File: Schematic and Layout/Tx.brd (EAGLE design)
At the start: 76.2 x 63.5 mm, 31 parts

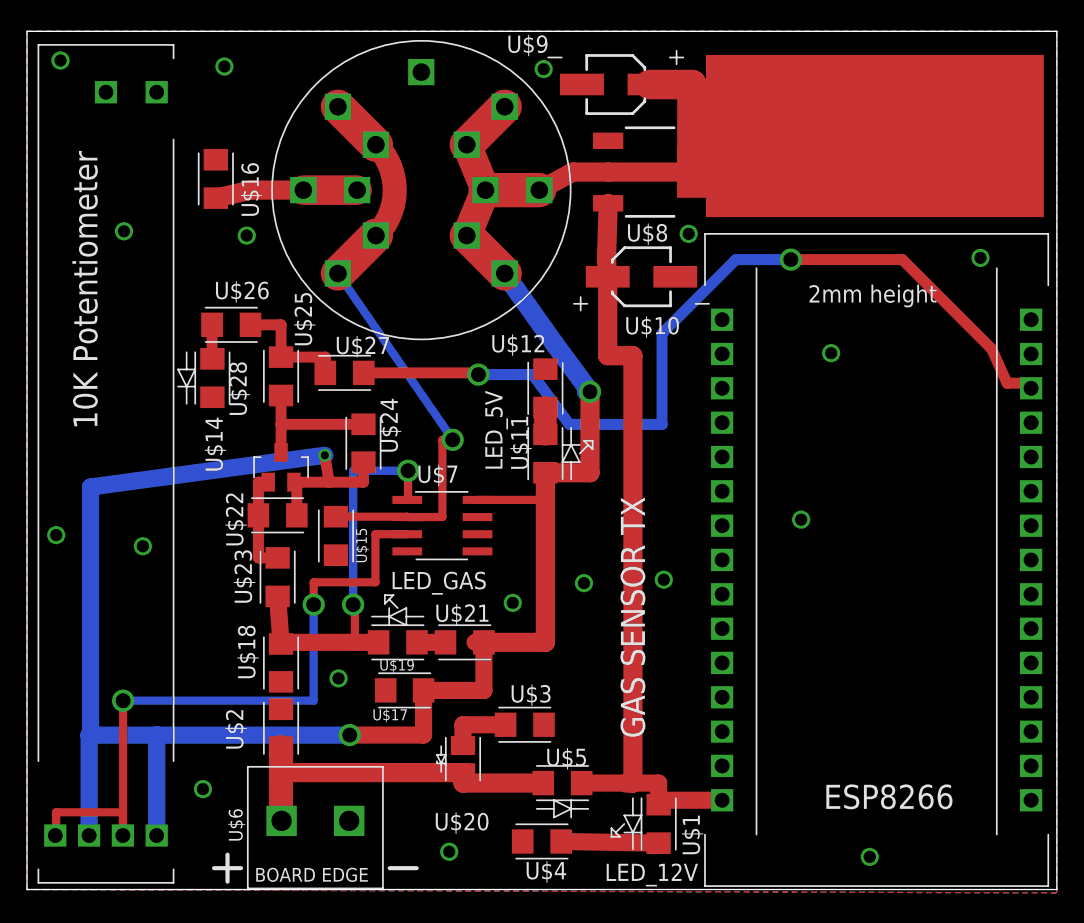
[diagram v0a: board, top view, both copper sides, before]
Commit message: ESPs now run off of 5 V
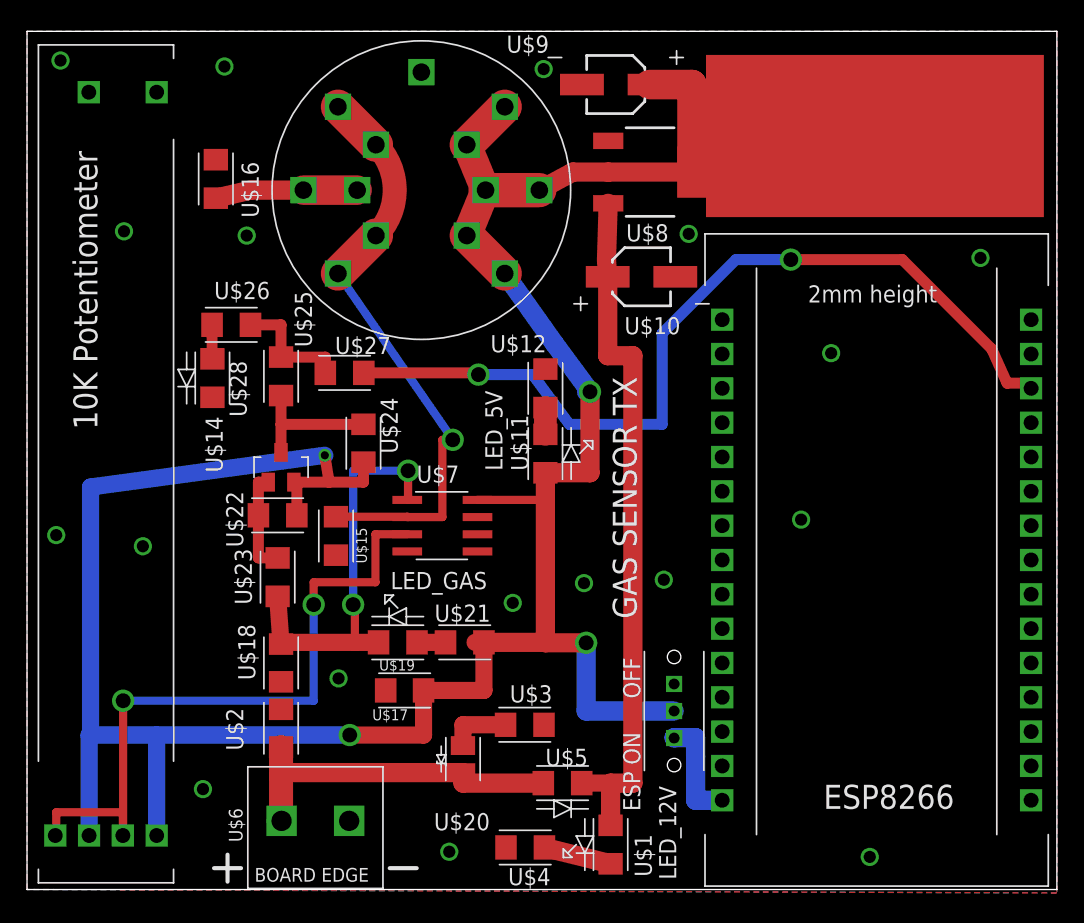
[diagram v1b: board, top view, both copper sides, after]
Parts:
- added U$32: SPDT, Gas_Sensor_Lib_v1:SPDT
- moved U$1 3.87 mm to (43.2, 3.33)
- moved U$4 1.32 mm to (36.9, 3.11)
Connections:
- new net ESP_VIN: U$29.VIN, U$32.A
- net 12V: no longer U$29.VIN
- net 5V: now also U$32.IN
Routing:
- net 5V: track 198.5 -> 213.0 mm, vias 3 -> 4
- net ESP_VIN: track 0.00 -> 8.25 mm
- net 12V: track 57.3 -> 52.8 mm
- net N$2: track 7.22 -> 5.04 mm
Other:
- board text added: "TRANSCEIVER - TX CAPSTONE SPRING 2017"
- board text removed: "TRANCEIVER - TX CAPSTONE SPRING 2017"
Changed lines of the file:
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@@
 <setting verticaltext="up"/>
 </settings>
-<grid distance="0.0025" unitdist="inch" unit="inch" style="dots" multiple="1" display="yes" altdistance="0.025" altunitdist="inch" altunit="inch"/>
+<grid distance="0.00125" unitdist="inch" unit="inch" style="dots" multiple="1" display="yes" altdistance="0.025" altunitdist="inch" altunit="inch"/>
 <layers>
 <layer number="1" name="Top" color="4" fill="1" visible="yes" active="yes"/>
@@
 <text x="5.207" y="34.036" size="1.778" layer="21" rot="R90">10K Potentiometer</text>
 <text x="58.928" y="5.969" size="1.778" layer="21">ESP8266</text>
-<text x="45.72" y="11.176" size="1.778" layer="21" rot="R90">GAS SENSOR TX</text>
-<text x="70.358" y="38.608" size="1.778" layer="22" rot="MR270">TRANCEIVER - TX
+<text x="45.11675" y="20.03425" size="1.778" layer="21" rot="R90">GAS SENSOR TX</text>
+<text x="70.358" y="38.608" size="1.778" layer="22" rot="MR270">TRANSCEIVER - TX
 CAPSTONE SPRING 2017</text>
 <text x="65.024" y="19.558" size="1.778" layer="22" rot="MR270">Alec
@@
 Kam
 Noah</text>
-<text x="42.7355" y="0.635" size="1.27" layer="21">LED_12V</text>
+<text x="48.03775" y="0.73025" size="1.27" layer="21" rot="R90">LED_12V</text>
 <text x="35.179" y="30.988" size="1.27" layer="21" rot="R90">LED_5V</text>
 <text x="34.036" y="23.495" size="1.27" layer="21" rot="R180">LED_GAS</text>
@@
 </autorouter>
 <elements>
-<element name="U$1" library="Gas_Sensor_Lib_v1" package="LED_1206" value="LED_12V" x="46.736" y="4.851" smashed="yes" rot="R270">
-<attribute name="NAME" x="48.514" y="5.613" size="1.27" layer="25" rot="R270"/>
-<attribute name="VALUE" x="42.647" y="0.635" size="1.27" layer="27"/>
+<element name="U$1" library="Gas_Sensor_Lib_v1" package="LED_1206" value="LED_12V" x="43.18" y="3.327" smashed="yes" rot="R270">
+<attribute name="NAME" x="44.958" y="4.089" size="1.27" layer="25" rot="R270"/>
+<attribute name="VALUE" x="49.911" y="0.76875" size="1.27" layer="27" rot="R90"/>
 </element>
 <element name="U$2" library="Gas_Sensor_Lib_v1" package="C1206" value="10uF" x="18.796" y="11.938" smashed="yes" rot="R90">
@@
 <attribute name="VALUE" x="42.164" y="14.478" size="1.27" layer="27" rot="R180"/>
 </element>
-<element name="U$4" library="Gas_Sensor_Lib_v1" package="R1206" value="1K" x="38.1" y="3.556" smashed="yes">
-<attribute name="NAME" x="36.83" y="0.762" size="1.27" layer="25"/>
-<attribute name="VALUE" x="34.163" y="0.762" size="1.27" layer="27"/>
+<element name="U$4" library="Gas_Sensor_Lib_v1" package="R1206" value="1K" x="36.86175" y="3.1115" smashed="yes">
+<attribute name="NAME" x="35.59175" y="0.3175" size="1.27" layer="25"/>
+<attribute name="VALUE" x="32.92475" y="0.3175" size="1.27" layer="27"/>
 </element>
 <element name="U$5" library="Gas_Sensor_Lib_v1" package="DIDOE_1206" value="DIODE" x="39.624" y="7.874" smashed="yes">
@@
 <element name="U$30" library="Gas_Sensor_Lib_v1" package="POTENTIOMETER" value="POTENTIOMETER" x="5.842" y="31.496" smashed="yes" rot="R90"/>
 <element name="U$31" library="Gas_Sensor_Lib_v1" package="THERMAL" value="HEAT_SINK" x="62.738" y="55.753"/>
+<element name="U$32" library="Gas_Sensor_Lib_v1" package="SPDT" value="SPDT" x="47.879" y="13.208" rot="R90"/>
 </elements>
 <signals>
@@
 <contactref element="U$8" pad="3"/>
 <contactref element="U$10" pad="+"/>
-<contactref element="U$29" pad="VIN"/>
-<wire x1="44.323" y1="7.874" x2="46.736" y2="7.874" width="1.27" layer="1"/>
-<wire x1="44.323" y1="7.874" x2="41.046" y2="7.874" width="1.27" layer="1"/>
-<wire x1="46.736" y1="6.604" x2="46.736" y2="7.874" width="1.27" layer="1"/>
-<wire x1="51.435" y1="6.604" x2="46.736" y2="6.604" width="1.27" layer="1"/>
-<wire x1="46.736" y1="6.604" x2="46.736" y2="6.273" width="1.27" layer="1"/>
+<wire x1="41.046" y1="7.874" x2="44.323" y2="7.874" width="1.27" layer="1"/>
 <wire x1="42.8752" y1="46.5728" x2="42.966" y2="45.339" width="1.4224" layer="1"/>
 <wire x1="42.8752" y1="46.5728" x2="43.0022" y2="50.7746" width="1.4224" layer="1"/>
@@
 <wire x1="44.831" y1="39.497" x2="44.831" y2="7.874" width="1.4224" layer="1"/>
 <wire x1="44.831" y1="7.874" x2="44.323" y2="7.874" width="1.4224" layer="1"/>
+<wire x1="44.323" y1="7.874" x2="43.18" y2="7.874" width="1.4224" layer="1"/>
+<wire x1="43.18" y1="7.874" x2="43.18" y2="4.749" width="1.4224" layer="1"/>
 </signal>
 <signal name="N$2">
 <contactref element="U$1" pad="2"/>
 <contactref element="U$4" pad="2"/>
-<wire x1="46.736" y1="3.429" x2="39.522" y2="3.556" width="1.27" layer="1"/>
+<wire x1="43.18" y1="1.905" x2="38.28375" y2="3.1115" width="1.4224" layer="1"/>
 </signal>
 <signal name="5V">
@@
 <wire x1="29.34" y1="11.43" x2="23.876" y2="11.43" width="1.27" layer="1"/>
 <wire x1="4.592" y1="3.996" x2="4.592" y2="11.43" width="1.27" layer="16"/>
-<wire x1="4.592" y1="11.43" x2="9.592" y2="11.43" width="1.27" layer="16"/>
+<wire x1="4.699" y1="11.43" x2="9.592" y2="11.43" width="1.27" layer="16"/>
 <contactref element="U$31" pad="P$1"/>
 <wire x1="49.2" y1="53.086" x2="43.0022" y2="53.086" width="1.4224" layer="1"/>
 <wire x1="59.436" y1="52.959" x2="62.738" y2="55.753" width="3.81" layer="1" curve="90"/>
-<wire x1="38.354" y1="30.836" x2="38.354" y2="18.288" width="1.4224" layer="1"/>
+<wire x1="38.354" y1="18.288" x2="38.354" y2="30.836" width="1.4224" layer="1"/>
 <wire x1="38.354" y1="18.288" x2="33.807" y2="18.288" width="1.4224" layer="1"/>
 <wire x1="38.354" y1="30.836" x2="38.354" y2="28.829" width="0.6096" layer="1"/>
@@
 <wire x1="19.746" y1="30.142" x2="19.964" y2="30.142" width="0.8128" layer="1"/>
 <wire x1="19.964" y1="30.142" x2="19.964" y2="27.686" width="0.8128" layer="1"/>
-<wire x1="24.892" y1="31.62" x2="24.892" y2="30.142" width="0.8128" layer="1"/>
+<wire x1="24.892" y1="30.142" x2="24.892" y2="31.62" width="0.8128" layer="1"/>
 <wire x1="22.352" y1="30.142" x2="24.892" y2="30.142" width="0.8128" layer="1"/>
 <wire x1="22.352" y1="30.142" x2="19.746" y2="30.142" width="0.8128" layer="1"/>
@@
 <via x="22.0345" y="32.131" extent="1-16" drill="0.6" shape="square"/>
 <wire x1="22.0345" y1="32.131" x2="22.352" y2="30.142" width="0.8128" layer="1"/>
+<contactref element="U$32" pad="IN"/>
+<wire x1="47.879" y1="13.208" x2="41.37025" y2="13.208" width="1.4224" layer="16"/>
+<wire x1="41.37025" y1="13.208" x2="41.37025" y2="18.25625" width="1.4224" layer="16"/>
+<via x="41.37025" y="18.25625" extent="1-16" drill="1.1" shape="square"/>
+<wire x1="41.37025" y1="18.25625" x2="38.354" y2="18.25625" width="1.4224" layer="1"/>
+<wire x1="38.354" y1="18.25625" x2="38.354" y2="18.288" width="1.4224" layer="1"/>
 </signal>
 <signal name="N$3">
@@
 <wire x1="30.734" y1="27.559" x2="28.134" y2="27.559" width="0.6096" layer="1"/>
 </signal>
+<signal name="ESP_VIN">
+<contactref element="U$29" pad="VIN"/>
+<wire x1="51.435" y1="6.63575" x2="51.435" y2="6.604" width="1.4224" layer="1"/>
+<contactref element="U$32" pad="A"/>
+<wire x1="49.4712" y1="9.8675125" x2="49.4665" y2="9.8722125" width="1.4224" layer="16"/>
+<wire x1="49.4665" y1="9.8722125" x2="49.4665" y2="11.2395" width="1.4224" layer="16"/>
+<wire x1="51.435" y1="6.604" x2="49.4712" y2="6.604" width="1.4224" layer="16"/>
+<wire x1="49.4712" y1="6.604" x2="49.4712" y2="9.8675125" width="1.4224" layer="16"/>
+<wire x1="49.4665" y1="11.2395" x2="47.879" y2="11.2395" width="1.4224" layer="16"/>
+<wire x1="47.879" y1="11.2395" x2="47.879" y2="11.208" width="1.4224" layer="16"/>
+</signal>
 </signals>

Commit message: Definitively added zener diodes
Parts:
- removed U$26: ?, Gas_Sensor_Lib_v1:R1206
- U$25: value ? -> 1K
- U$28: value DIODE_1206 -> DIODE_Z_3.3V; device Gas_Sensor_Lib_v1:DIDOE_1206 -> Gas_Sensor_Lib_v1:SOD-323
- moved U$28 1.99 mm to (15.0, 39.4), turned to 0 degrees
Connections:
- removed net N$12: U$26.1, U$28.1
- net GND: now also U$28.P$1; no longer U$28.2
- net N$13: now also U$28.P$2; no longer U$26.2
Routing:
- net N$12: track 2.54 -> 0.00 mm
- net N$13: track 9.32 -> 7.42 mm
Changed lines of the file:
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@@
 <attribute name="VALUE" x="23.114" y="30.988" size="1.27" layer="27" rot="R90"/>
 </element>
-<element name="U$25" library="Gas_Sensor_Lib_v1" package="R1206" value="?" x="18.796" y="37.973" smashed="yes" rot="R270">
+<element name="U$25" library="Gas_Sensor_Lib_v1" package="R1206" value="1K" x="18.796" y="37.973" smashed="yes" rot="R270">
 <attribute name="NAME" x="21.082" y="40.132" size="1.27" layer="25" rot="R90"/>
 <attribute name="VALUE" x="19.939" y="36.576" size="1.27" layer="27"/>
-</element>
-<element name="U$26" library="Gas_Sensor_Lib_v1" package="R1206" value="?" x="15.113" y="41.783" smashed="yes">
-<attribute name="NAME" x="13.843" y="43.688" size="1.27" layer="25"/>
-<attribute name="VALUE" x="13.843" y="45.593" size="1.27" layer="27"/>
 </element>
 <element name="U$27" library="Gas_Sensor_Lib_v1" package="R1206" value="1K" x="23.495" y="38.227" smashed="yes" rot="R180">
@@
 <attribute name="VALUE" x="24.511" y="36.957" size="1.27" layer="27" rot="R180"/>
 </element>
-<element name="U$28" library="Gas_Sensor_Lib_v1" package="DIDOE_1206" value="DIODE_1206" x="13.716" y="37.846" smashed="yes" rot="R270">
-<attribute name="NAME" x="14.986" y="39.116" size="1.27" layer="25" rot="R270"/>
-<attribute name="VALUE" x="9.525" y="39.878" size="1.27" layer="27" rot="R270"/>
-</element>
 <element name="U$29" library="Gas_Sensor_Lib_v1" package="ESP" value="ESP8266" x="62.865" y="24.384" smashed="yes"/>
 <element name="U$30" library="Gas_Sensor_Lib_v1" package="POTENTIOMETER" value="POTENTIOMETER" x="5.842" y="31.496" smashed="yes" rot="R90"/>
 <element name="U$31" library="Gas_Sensor_Lib_v1" package="THERMAL" value="HEAT_SINK" x="62.738" y="55.753"/>
 <element name="U$32" library="Gas_Sensor_Lib_v1" package="SPDT" value="SPDT" x="47.879" y="13.208" rot="R90"/>
+<element name="U$28" library="Gas_Sensor_Lib_v1" package="SOD-323" value="DIODE_Z_3.3V" x="14.95425" y="39.40175"/>
 </elements>
 <signals>
@@
 <contactref element="U$17" pad="2"/>
 <contactref element="U$18" pad="1"/>
-<contactref element="U$28" pad="2"/>
 <contactref element="U$29" pad="GND_0"/>
 <contactref element="U$29" pad="GND_3"/>
@@
 <via x="23.0505" y="15.621" extent="1-16" drill="0.9" shape="square"/>
 <via x="2.4765" y="61.341" extent="1-16" drill="0.9" shape="square"/>
+<contactref element="U$28" pad="P$1"/>
 </signal>
 <signal name="12V_IN">
@@
 <wire x1="24.892" y1="34.417" x2="18.796" y2="34.417" width="0.8128" layer="1"/>
 </signal>
-<signal name="N$12">
-<contactref element="U$28" pad="1"/>
-<contactref element="U$26" pad="1"/>
-<wire x1="13.691" y1="41.783" x2="13.691" y2="39.268" width="0.8128" layer="1"/>
-<wire x1="13.691" y1="39.268" x2="13.716" y2="39.268" width="0.8128" layer="1"/>
-</signal>
 <signal name="N$13">
-<contactref element="U$26" pad="2"/>
 <contactref element="U$25" pad="1"/>
 <contactref element="U$27" pad="2"/>
 <wire x1="19.025" y1="39.395" x2="18.796" y2="39.395" width="0.8128" layer="1"/>
-<wire x1="16.535" y1="41.783" x2="18.796" y2="41.783" width="0.8128" layer="1"/>
-<wire x1="18.796" y1="41.783" x2="18.796" y2="39.395" width="0.8128" layer="1"/>
 <wire x1="18.796" y1="39.395" x2="22.073" y2="39.395" width="0.8128" layer="1"/>
 <wire x1="22.073" y1="39.395" x2="22.073" y2="38.227" width="0.8128" layer="1"/>
+<contactref element="U$28" pad="P$2"/>
+<wire x1="18.796" y1="39.395" x2="16.05425" y2="39.395" width="1.4224" layer="1"/>
+<wire x1="16.05425" y1="39.395" x2="16.05425" y2="39.40175" width="1.4224" layer="1"/>
 </signal>
 <signal name="N$14">
